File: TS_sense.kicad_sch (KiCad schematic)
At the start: 28 parts, among them U11 OPA355NA, U13 SFH617A-1X007T

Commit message: Changed Layout
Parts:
- added U16: TBA1-0511E, Converter_DCDC:Converter_DCDC_TRACO_TBA1-xxxxE_Single_THT, symbol Converter_DCDC:TBA1-0511E
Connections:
- net +5V_{iso}: now also U16.6 (+Vout)
- net GND: now also U16.2 (-Vin)
- net  HV+ renamed TS+
- net HV- renamed TS-
- net TS-: now also U16.4 (-Vout)
- new net +5V: U16.1 (+Vin)
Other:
- note added: "ISO 1.5kV"
- note added: "ISO 3750kV_{rms}"
- note added: "LVS"
- note added: "TS VOLTAGE AREA"
- note removed: "Footprint Check"

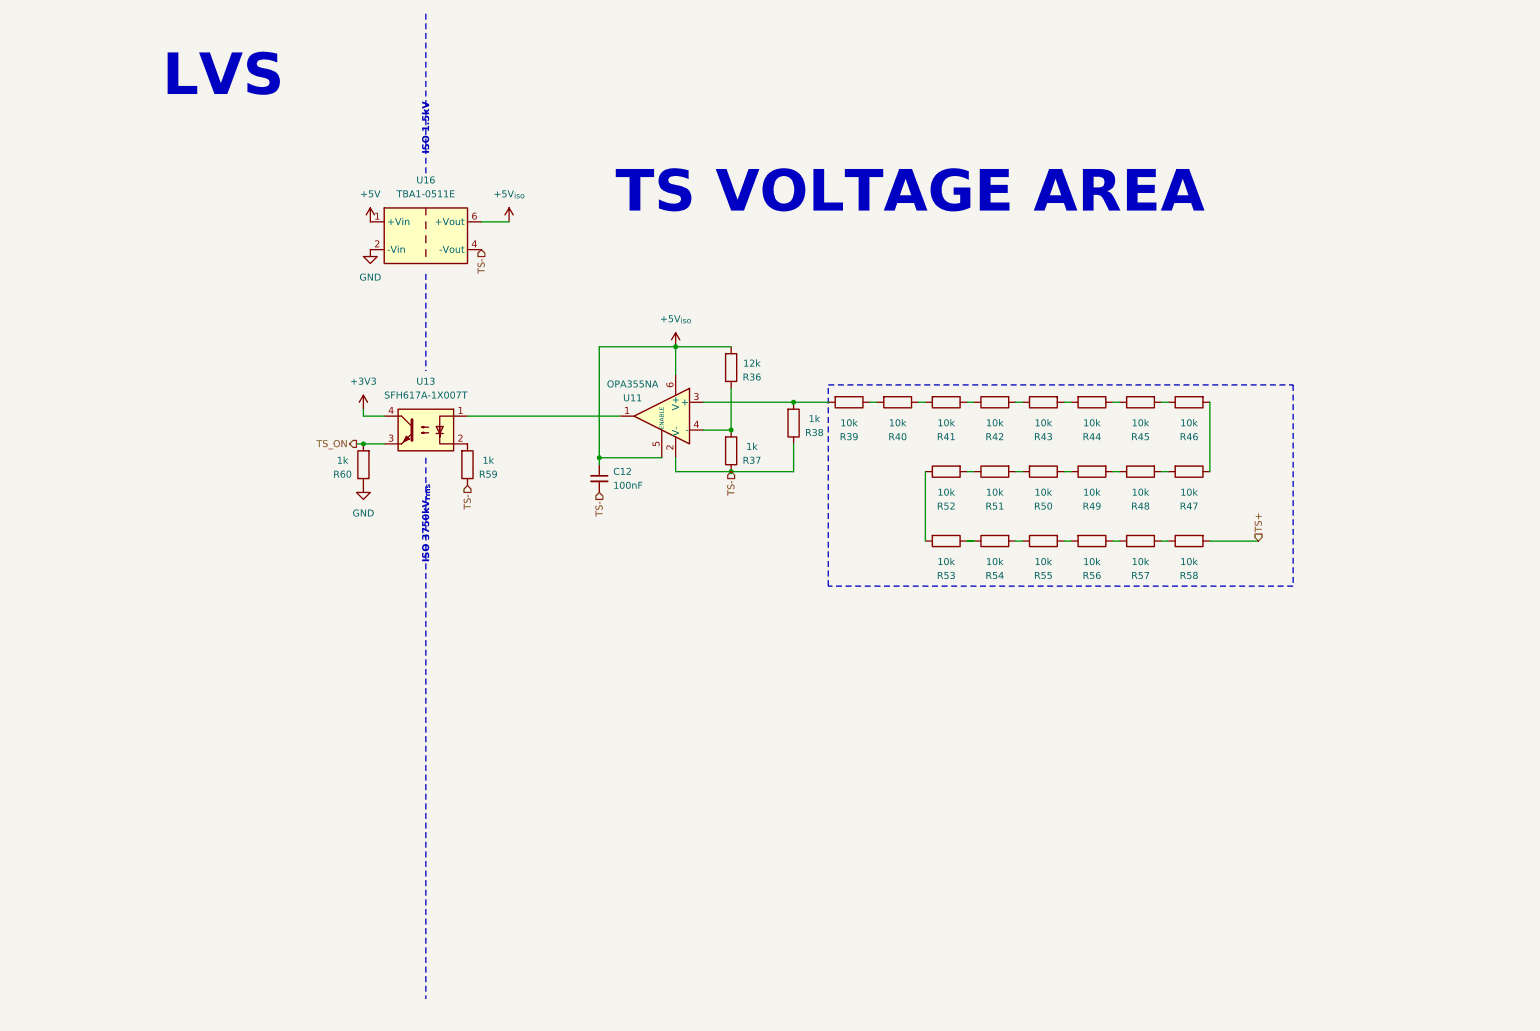
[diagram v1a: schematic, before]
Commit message: Added decoupling Caps
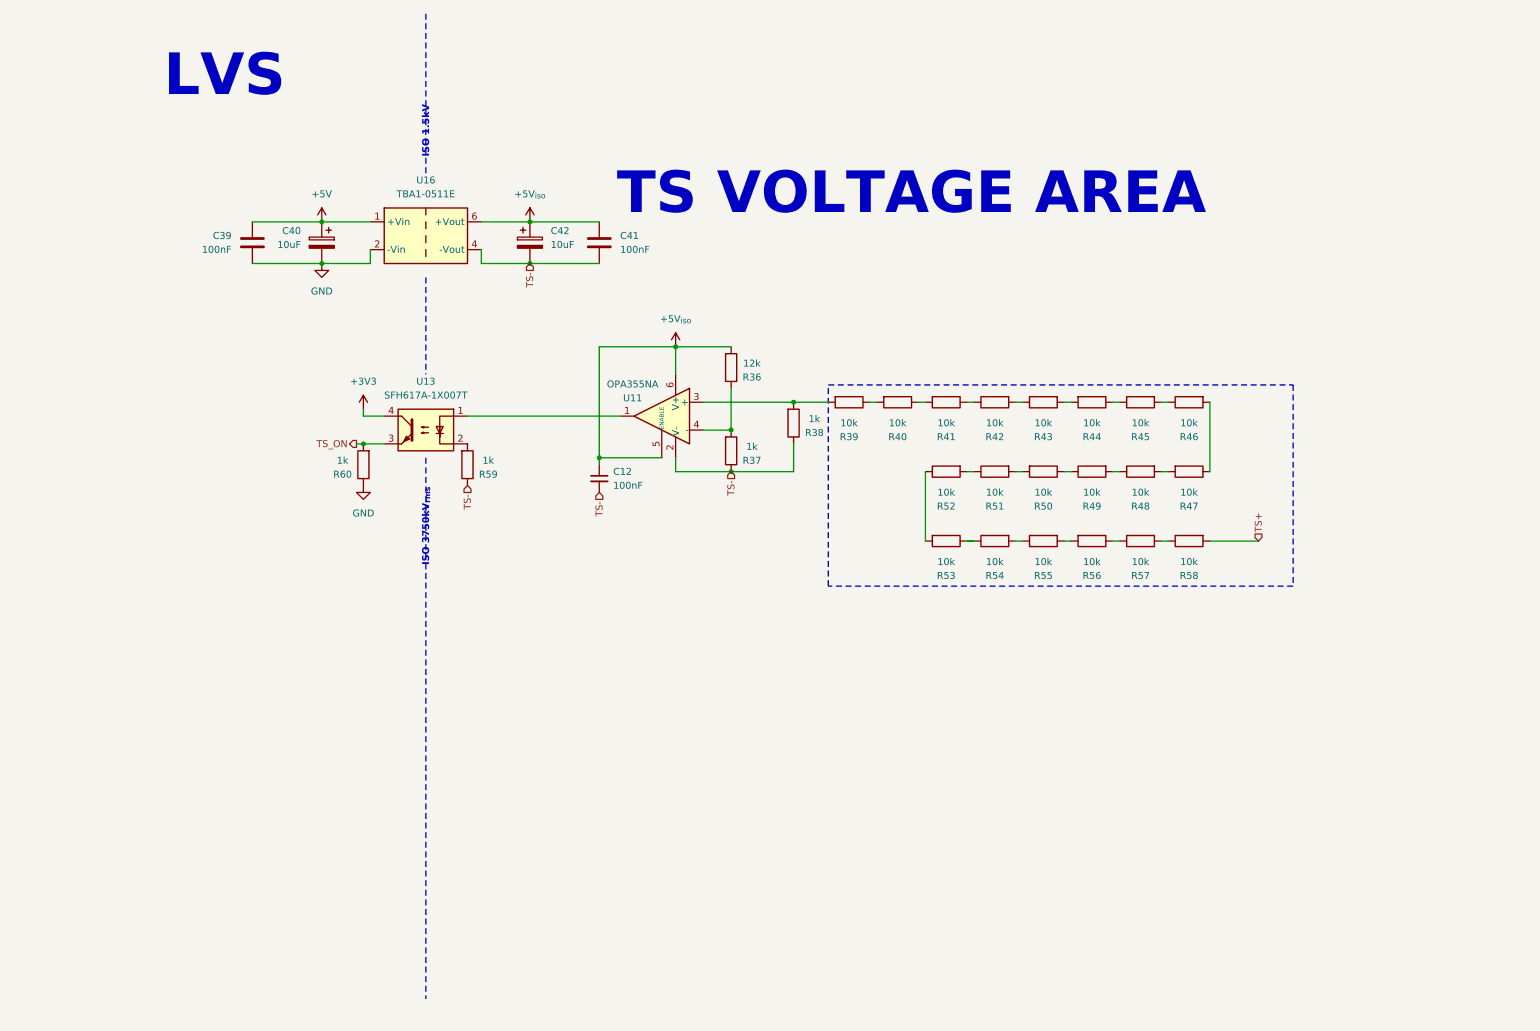
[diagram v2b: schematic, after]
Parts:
- added C39, C41: 100nF, symbol Device:C
- added C40, C42: 10uF, symbol Device:C_Polarized
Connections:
- net +5V: now also C39.1, C40.1
- net +5V_{iso}: now also C41.1, C42.1
- net GND: now also C39.2, C40.2
- net TS-: now also C41.2, C42.2

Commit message: Added Rules
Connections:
- net +3V3 is gone; now on net +5V: U13.4
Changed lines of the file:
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@@
 	(text "TS VOLTAGE AREA"
 		(exclude_from_sim no)
-		(at 171.45 45.72 0)
+		(at 175.006 24.13 0)
 		(effects
 			(font
@@
 	)
 	(symbol
-		(lib_id "power:+3V3")
+		(lib_id "power:+5V")
 		(at 71.12 85.09 0)
 		(unit 1)
@@
 			)
 		)
-		(property "Value" "+3V3"
+		(property "Value" "+5V"
 			(at 71.12 80.01 0)
 			(effects
@@
 			)
 		)
-		(property "Description" "Power symbol creates a global label with name \"+3V3\""
+		(property "Description" "Power symbol creates a global label with name \"+5V\""
 			(at 71.12 85.09 0)
 			(effects
@@
 		)
 		(instances
-			(project ""
+			(project "rpm_TSAL"
 				(path "/d61aec95-1a95-4bdc-98ef-7f05cebfb826/3d691545-fb91-40e8-bbf0-202d017ae861"
 					(reference "#PWR050")

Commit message: Submission Ready. ESF 15.07.24
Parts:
- removed R39, R40, R41, R42, R43, R44, R45, R46, R47, R48, R49, R50, R51, R52, R53, R54, R55, R56, R57, R58: 10k, Resistor_SMD:R_0603_1608Metric, symbol Device:R
- added R10, R11, R12, R13, R8, R9: 52k3, Resistor_SMD:R_0805_2012Metric, symbol Device:R
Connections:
- net TS+: now also R13.1
- net at R38.2, U11.3 (+): now also R8.2
- new net: R10.1, R11.1
- new net: R11.2, R12.1
- new net: R12.2, R13.2
- new net: R10.2, R9.1
- new net: R8.1, R9.2
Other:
- note added: "Resistor Datasheet"

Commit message: ⠀⠀⠀⠀⠀⠀⠀⠀⠀⠀⠀⠀⠀⠀⠀⠀⠀⠀⠀⠀⠀⠀⠀⠀⠀⠀⠀⠀⠀⠀⠀⠀⠀⠀⠀⠀⠀⣠⣤⣤⣤⡀⠀⠀⠀⠀⠀⠀⠀⠀⠀⠀⠀⠀⠀⠀⠀⠀⠀⠀⠀⠀⠀⠀⠀ ⠀⠀⠀⠀⠀⠀⠀⠀⠀⠀⠀⠀⠀⠀⠀⠀⠀⠀⠀⠀⠀⠀⠀⠀⠀⠀⠀⠀⠀⠀⠀⠀⠀⠀⣠⣶⣿⠟⠉⠉⠻⣿⡄⠀⠀⠀⠀⠀⠀⠀⠀⠀⠀⠀⠀⠀⠀⠀⠀⠀⠀⠀⠀⠀⠀ ⠀⠀⠀⠀⠀⠀⠀⠀⠀⠀⠀⠀⠀⠀⠀⠀⠀⠀⠀⠀⠀⠀⠀⠀⠀⠀⠀⠀⠀⠀⠀⢀⣤⣾⠿⠉⠀⠀⠀⠀⠀⠹⣿⡄⠀⠀⠀⠀⠀⠀⠀⠀⠀⠀⠀⠀⠀⠀⠀⠀⠀⠀⣀⣴⣾ ⠀⠀⠀⠀⠀⠀⠀⠀⠀⠀⠀⠀⠀⠀⠀⠀⠀⠀⠀⠀⠀⠀⠀⠀⠀⠀⠀⠀⠀⢀⣴⣿⠟⠁⠀⠀⠀⠀⠀⠀⠀⠀⣿⣿⠀⠀⠀⠀⠀⠀⠀⠀⠀⠀⠀⠀⠀⠀⠀⣀⣴⣾⡿⠛⠉ ⠀⠀⠀⠀⠀⠀⠀⠀⠀⠀⠀⠀⠀⠀⠀⠀⠀⠀⠀⠀⠀⠀⠀⠀⠀⠀⠀⢀⣴⣿⠟⠁⠀⠀⠀⠀⠀⠀⠀⠀⠀⠀⢸⣿⡆⠀⠀⠀⠀⠀⠀⠀⠀⠀⠀⠀⢀⣴⣾⡿⠟⠁⠀⠀⠀ ⠀⠀⠀⠀⠀⠀⠀⠀⠀⠀⠀⠀⠀⠀⠀⠀⠀⠀⠀⠀⠀⠀⠀⠀⢀⣀⣴⣿⡿⠃⠀⠀⠀⠀⠀⠀⠀⠀⠀⠀⠀⠀⢸⣿⣷⣶⣶⣦⣤⣤⣄⡀⠀⢀⣠⣾⣿⠿⠋⠀⠀⠀⠀⠀⣠ ⠀⠀⠀⠀⠀⠀⠀⠀⠀⠀⠀⠀⠀⠀⠀⠀⠀⠀⠀⠀⠀⠀⠀⣼⣿⣿⡿⠋⠀⠀⠀⠀⠀⠀⠀⠀⠀⠀⠀⣠⣤⠶⠞⣿⠟⠋⠉⠉⠙⣻⠿⢿⣿⣿⣿⠟⠁⠀⠀⠀⠀⠀⢀⡼⠁ ⠀⠀⠀⠀⠀⠀⠀⠀⠀⠀⠀⠀⠀⠀⠀⠀⠀⠀⠀⠀⠀⠀⢰⣿⠁⠛⠀⠀⠀⠀⠀⠀⠀⠀⠀⠀⠀⠀⣰⠟⠁⢠⡞⠁⠀⠀⠀⢀⡴⠋⠀⢀⡿⠋⠁⠀⠀⠀⠀⠀⠀⠀⡞⠁⠀ ⠀⠀⠀⠀⠀⠀⠀⠀⠀⠀⠀⠀⠀⠀⠀⠀⠀⠀⠀⠀⠀⣠⣼⣿⡄⠀⠀⠀⠀⠀⠀⠀⠀⠀⠀⠀⠀⣼⠃⠀⢠⠏⠀⠀⠀⠀⣰⠏⠀⠀⣠⠟⠀⠀⠀⠀⠀⠀⠀⠀⠀⢸⡥⠤⡀ ⠀⠀⠀⠀⠀⠀⠀⠀⠀⠀⠀⠀⠀⠀⠀⠀⠀⠀⠀⠀⣰⣿⠟⠁⠀⠀⠀⠀⠀⠀⠀⠀⠀⠀⠀⠀⠠⣇⠀⣠⡏⠀⠀⠀⠀⣼⠁⠀⠀⣰⠋⠀⠀⠀⠀⠀⠀⠀⠀⠀⠀⠀⢀⡴⠁ ⠀⠀⠀⠀⠀⠀⠀⠀⠀⠀⠀⠀⠀⠀⠀⠀⣀⣄⣄⣼⣿⠋⠀⠀⠀⠀⠀⠀⠀⠀⠀⠀⠀⠀⠀⠀⠀⢻⡶⠋⠀⠀⠀⠀⢸⣧⠀⠀⣴⠃⠀⠀⠀⠀⠀⠀⠀⠀⠀⠀⠀⠀⠘⢧⠀ ⠀⠀⠀⠀⠀⠀⠀⠀⢀⣀⣀⠀⠀⠀⠀⣾⡿⠿⣿⡿⠁⠀⠀⠀⠀⠀⠀⣠⣶⣶⣶⡀⠀⠀⠀⠀⠀⠀⠀⠀⠀⠀⠀⠀⠀⠙⠛⠛⠁⠀⠀⠀⠀⠀⠀⠀⠀⠀⠀⠀⠀⠀⠀⠈⠳ ⠀⠀⠀⠀⠀⠀⢀⣾⠿⠛⢿⣿⣷⣄⡀⣿⠃⠀⠈⠀⠀⠀⠀⠀⠀⢀⣾⣿⣿⣿⣿⣧⠀⠀⠀⠀⠀⠀⠀⠀⠀⠀⠀⠀⠀⠀⠀⠀⠀⠀⠀⠀⠀⠀⠀⠀⠀⠀⠀⠀⠀⠀⠀⠀⠀ ⠀⠀⠀⣠⣤⣦⣼⣿⠀⠀⠀⣿⣿⣿⣿⣿⣦⣀⠀⠀⠀⠀⠀⠀⠀⣿⣿⣿⣿⣿⣿⡿⠀⠀⠀⢀⣀⣀⣀⣀⡀⠀⠀⠀⠀⠀⠀⠀⠀⠀⠀⣤⣾⣿⣿⣿⣷⣄⠀⠀⠀⠀⠀⠀⠀ ⠀⣠⣾⡿⠋⠉⠉⠁⠀⠀⠀⠀⠉⢯⡙⠻⣿⣿⣷⣤⡀⠀⠀⠀⠀⢿⣿⣿⣿⣿⡿⠃⢀⡤⠖⠋⠉⠉⠉⠉⠉⠉⠒⠦⣄⠀⠀⠀⠀⠀⣾⣿⣿⣿⣿⣿⣿⣿⣧⠀⠀⠀⠀⠀⠀ ⣾⣿⠋⠀⠀⠀⠀⣀⣀⠀⠀⠀⠀⠀⠙⢦⣄⠉⠻⢿⣿⣷⣦⡀⠀⠈⠙⠛⠛⠋⠀⢰⠟⡇⠀⠀⠀⠀⠀⠀⠀⠀⠀⠀⠈⠳⣄⠀⠀⠀⣿⣿⣿⣿⣿⣿⣿⣿⣿⠀⠀⠀⠀⠀⠀ ⣿⡇⠀⠀⠀⣴⠟⣫⣿⣿⣄⠀⠀⠀⠀⡶⢌⡙⠶⣤⡈⠛⠿⣿⣷⣦⣀⠀⠀⠀⠀⡇⠀⢻⣄⠀⠀⣠⢷⠀⠀⠀⠀⠀⡶⠀⠘⡆⠀⠀⠻⣿⣿⣿⣿⣿⣿⣿⡟⠀⠀⠀⠀⠀⠀ ⣿⡇⠀⠀⢸⣟⢸⣿⣿⣿⣿⠀⠀⠀⠀⡇⠀⠈⠛⠦⣝⡳⢤⣈⠛⠻⣿⣷⣦⣀⠀⠀⠀⠀⠈⠙⠋⠁⠀⠛⠦⠤⠤⠚⠁⠀⠀⢳⠀⠀⠀⠈⠛⠿⠿⠿⠟⠋⠀⠀⠀⠀⠀⠀⠀ ⣿⡇⠀⠀⠈⢿⣞⣿⣿⣿⠏⠀⠀⠀⠀⡇⠀⠀⠀⠀⠀⠙⠳⢬⣛⠦⠀⠙⢻⣿⣷⣦⣀⠀⠀⠀⠀⠀⠀⠀⠀⠀⠀⠀⠀⠀⠀⡞⠀⠀⠀⠀⠀⠀⠀⠀⠀⠀⠀⠀⠀⠀⠀⠀⠀ ⣿⡇⠀⠀⠀⠀⠉⠛⠋⠁⠀⠀⠀⠀⠀⡇⠀⠀⠀⠀⠀⠀⠀⠀⠈⠁⠀⠀⠈⣿⠉⢻⣿⣷⣦⣀⠀⠀⠀⠀⠀⠀⠀⠀⠀⢀⡼⠁⠀⠀⠀⠀⠀⠀⠀⠀⠀⠀⠀⠀⠀⠀⠀⠀⠀ ⣿⡇⠀⠀⠀⠀⠀⣠⣄⠀⠀⢰⠶⠒⠒⢧⣄⡀⠀⠀⠀⠀⠀⠀⠀⠀⠀⠀⠀⣿⠀⢸⡇⢸⡟⢿⣷⣦⣴⣶⣶⣶⣶⣤⣔⠋⠀⠀⠀⠀⠀⠀⠀⠀⠀⠀⠀⠀⠀⠀⠀⠀⠀⠀⠀ ⣿⡇⠀⠀⣤⠀⠀⠿⠿⠁⢀⡿⠀⠀⠀⡄⠈⠙⡷⢦⣄⡀⠀⠀⠀⠀⠀⠀⠀⣿⠀⢸⡇⢸⡇⠀⣿⠙⣿⣿⣉⠉⠙⠿⣿⣧⠀⠀⠀⠀⠀⠀⠀⠀⠀⠀⠀⠀⠀⠀⠀⠀⠀⠀⠀ ⣿⡇⠀⠀⠙⠷⢤⣀⣠⠴⠛⠁⠀⠀⠀⠇⠀⠀⡇⢸⡏⢹⡷⢦⣄⡀⠀⠀⠀⣿⡀⢸⡇⢸⡇⠀⡟⠀⢸⠀⢹⡷⢦⣄⣘⣿⡆⠀⠀⠀⠀⠀⠀⠀⠀⠀⠀⠀⠀⠀⠀⠀⠀⠀⠀ ⣿⣿⠢⣤⡀⠀⠀⠀⠀⠀⠀⣠⠾⣿⣿⡷⣤⣀⡇⠸⡇⢸⡇⢸⠉⠙⠳⢦⣄⡻⢿⣾⣧⣸⣧⠀⡇⠀⢸⠀⢸⡇⢤⣈⠙⠻⣿⣆⠀⠀⠀⠀⠀⠀⠀⠀⠀⠀⠀⠀⠀⠀⠀⠀⠀ ⢹⣿⣷⣌⡉⠛⠲⢶⣶⠖⠛⠛⢶⣄⡉⠛⠿⣽⣿⣶⣧⣸⡇⢸⠀⠀⠀⠀⠈⠙⠲⢮⣝⠻⣿⣷⣷⣄⣸⠀⢸⡇⠀⠈⠁⠀⢸⣿⠀⠀⠀⠀⠀⠀⠀⠀⠀⠀⠀⠀⠀⠀⠀⠀⠀ ⠀⠈⠙⠻⢿⣷⣶⣤⣉⡻⢶⣄⣀⠈⠙⠳⢦⣈⡉⠻⢿⣿⣷⣾⣦⡀⠀⠀⠀⠀⠀⠀⠈⠙⠲⢭⣛⠿⣿⣷⣼⡇⠀⠀⠀⠀⠈⣿⡇⠀⠀⠀⠀⠀⠀⣀⠀⠀⠀⠀⠀⠀⠀⠀⣀ ⠀⠀⠀⠀⠀⠈⠙⠻⢿⣿⣷⣶⣽⣻⡦⠀⠀⠈⠙⠷⣦⣌⡙⠻⢿⣟⣷⣤⣀⠀⠀⠀⠀⠀⠀⠀⠈⠙⠳⢯⣻⡇⠀⠀⠀⠀⠀⢸⣿⠀⣀⠀⠀⠀⠀⠈⠳⣄⠀⠀⠀⢀⡏⠙⠛ ⠀⠀⠀⠀⠀⠀⠀⠀⠀⠈⠛⠻⢿⣿⣿⣿⣶⣤⣤⣤⣀⣈⠛⠷⣤⣈⡛⠷⢽⡻⢶⣄⣀⠀⠀⠀⠀⠀⠀⠀⠈⠛⠳⢤⣀⠀⠀⢸⣿⡀⠈⠳⢤⣀⣀⣰⠃⠈⠛⠶⠶⠿⠃⠀⠀ ⠀⠀⠀⠀⠀⠀⠀⠀⠀⠀⠀⠀⠀⢈⣿⡿⠛⠉⠙⠛⠛⠻⢷⣦⣄⣩⣿⠶⠖⠛⠛⠛⠛⠛⠛⠿⢷⣶⣦⣄⠀⠀⠀⠀⠉⢻⣶⣿⣿⠇⠀⠀⠀⠉⠉⠀⠀⠀⠀⠀⠀⠀⠀⠀⠀ ⠀⠀⠀⠀⠀⠀⠀⠀⠀⠀⠀⠀⠀⣼⣿⠁⠀⠀⠀⠀⠀⠀⠀⣿⣿⠋⠀⠀⠀⠀⠀⣠⠖⠂⠀⠀⠀⠈⠙⠿⣿⣦⡄⠀⠀⣸⣿⠟⠋⠀⠀⠀⠀⠀⠀⠀⠀⠀⠀⠀⠀⠀⠀⠀⠀ ⠀⠀⠀⠀⠀⠀⠀⠀⠀⠀⠀⠀⢰⣿⡟⠀⠀⠀⠀⠀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
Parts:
- C39, C40, C41, C42: footprint (none) -> Capacitor_SMD:C_0603_1608Metric
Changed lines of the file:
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@@
 			)
 		)
-		(property "Footprint" ""
+		(property "Footprint" "Capacitor_SMD:C_0603_1608Metric"
 			(at 115.2652 58.42 0)
 			(effects
@@
 			)
 		)
-		(property "Footprint" ""
+		(property "Footprint" "Capacitor_SMD:C_0603_1608Metric"
 			(at 62.5348 58.42 0)
 			(effects
@@
 			)
 		)
-		(property "Footprint" ""
+		(property "Footprint" "Capacitor_SMD:C_0603_1608Metric"
 			(at 49.8348 58.42 0)
 			(effects
@@
 			)
 		)
-		(property "Footprint" ""
+		(property "Footprint" "Capacitor_SMD:C_0603_1608Metric"
 			(at 102.5652 58.42 0)
 			(effects

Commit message: TSAL Rev 0.2
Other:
- moved on the sheet: R38
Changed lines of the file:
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@@
 		(title "TSAL")
 		(date "2024-07-11")
-		(rev "V0.1")
+		(rev "V0.2")
 		(company "Team RPM - UAS Münster")
 		(comment 1 "Luca Sapion")
@@
 	)
 	(junction
-		(at 138.43 96.52)
-		(diameter 0)
-		(color 0 0 0 0)
-	)
-	(junction
 		(at 71.12 91.44)
 		(diameter 0)
@@
 	)
 	(junction
+		(at 138.43 97.79)
+		(diameter 0)
+		(color 0 0 0 0)
+	)
+	(junction
 		(at 101.6 50.8)
 		(diameter 0)
@@
 	(wire
 		(pts
+			(xy 138.43 97.79) (xy 138.43 96.52)
+		)
+		(stroke
+			(width 0)
+			(type default)
+		)
+	)
+	(wire
+		(pts
 			(xy 92.71 50.8) (xy 101.6 50.8)
 		)
@@
 	(wire
 		(pts
+			(xy 138.43 100.33) (xy 138.43 97.79)
+		)
+		(stroke
+			(width 0)
+			(type default)
+		)
+	)
+	(wire
+		(pts
+			(xy 149.86 86.36) (xy 149.86 83.82)
+		)
+		(stroke
+			(width 0)
+			(type default)
+		)
+	)
+	(wire
+		(pts
 			(xy 125.73 93.98) (xy 114.3 93.98)
 		)
@@
 	(wire
 		(pts
-			(xy 128.27 93.98) (xy 128.27 96.52)
+			(xy 128.27 93.98) (xy 128.27 97.79)
 		)
 		(stroke
@@
 	(wire
 		(pts
-			(xy 128.27 96.52) (xy 138.43 96.52)
+			(xy 128.27 97.79) (xy 138.43 97.79)
 		)
 		(stroke
@@
 	(wire
 		(pts
-			(xy 138.43 96.52) (xy 149.86 96.52)
+			(xy 138.43 97.79) (xy 149.86 97.79)
 		)
 		(stroke
@@
 	(wire
 		(pts
-			(xy 149.86 96.52) (xy 149.86 91.44)
+			(xy 149.86 97.79) (xy 149.86 93.98)
 		)
 		(stroke
@@
 	(hierarchical_label "TS-"
 		(shape input)
-		(at 138.43 96.52 270)
+		(at 138.43 100.33 270)
 		(fields_autoplaced yes)
 		(effects
@@
 	(symbol
 		(lib_id "Device:R")
-		(at 149.86 87.63 0)
+		(at 149.86 90.17 0)
 		(mirror x)
 		(unit 1)
@@
 		(dnp no)
 		(property "Reference" "R38"
+			(at 153.67 91.948 0)
+			(effects
+				(font
+					(size 1.27 1.27)
+				)
+			)
+		)
+		(property "Value" "1k"
 			(at 153.67 89.408 0)
 			(effects
@@
 			)
 		)
-		(property "Value" "1k"
-			(at 153.67 86.868 0)
-			(effects
-				(font
-					(size 1.27 1.27)
-				)
-			)
-		)
 		(property "Footprint" "Resistor_SMD:R_0603_1608Metric"
-			(at 148.082 87.63 90)
+			(at 148.082 90.17 90)
 			(effects
 				(font
@@
 		)
 		(property "Datasheet" "~"
-			(at 149.86 87.63 0)
+			(at 149.86 90.17 0)
 			(effects
 				(font
@@
 		)
 		(property "Description" "Resistor"
-			(at 149.86 87.63 0)
-			(effects
-				(font
+			(at 149.86 90.17 0)
+			(effects
+				(font

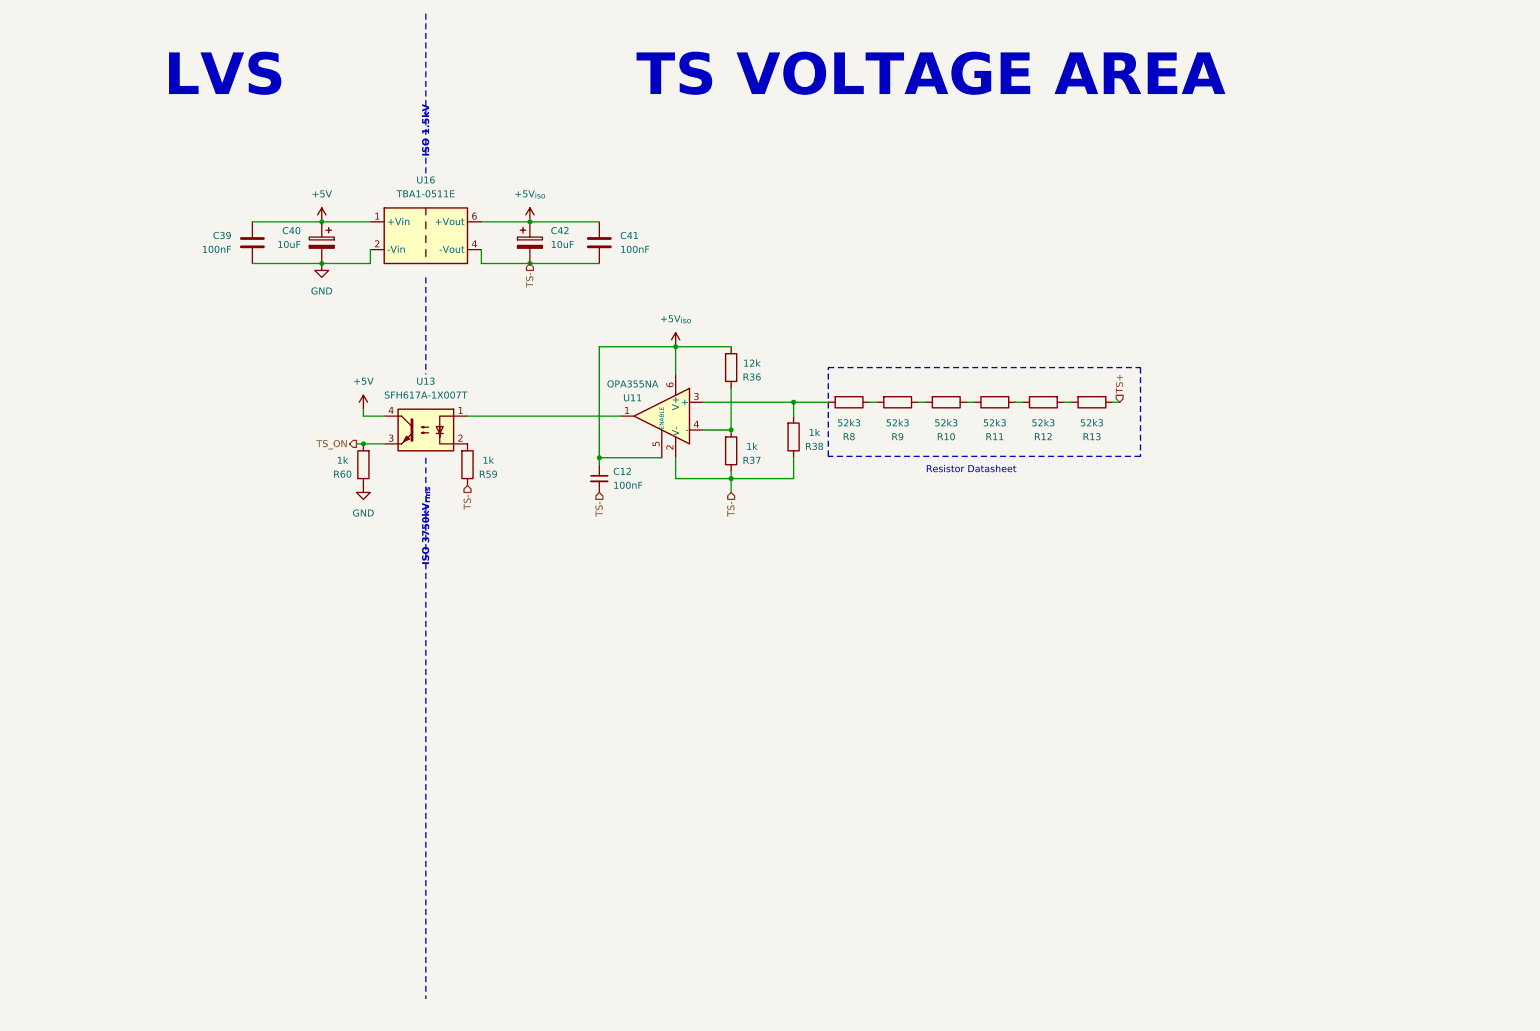
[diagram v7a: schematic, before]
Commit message: Added TSAC Indicator with PSU
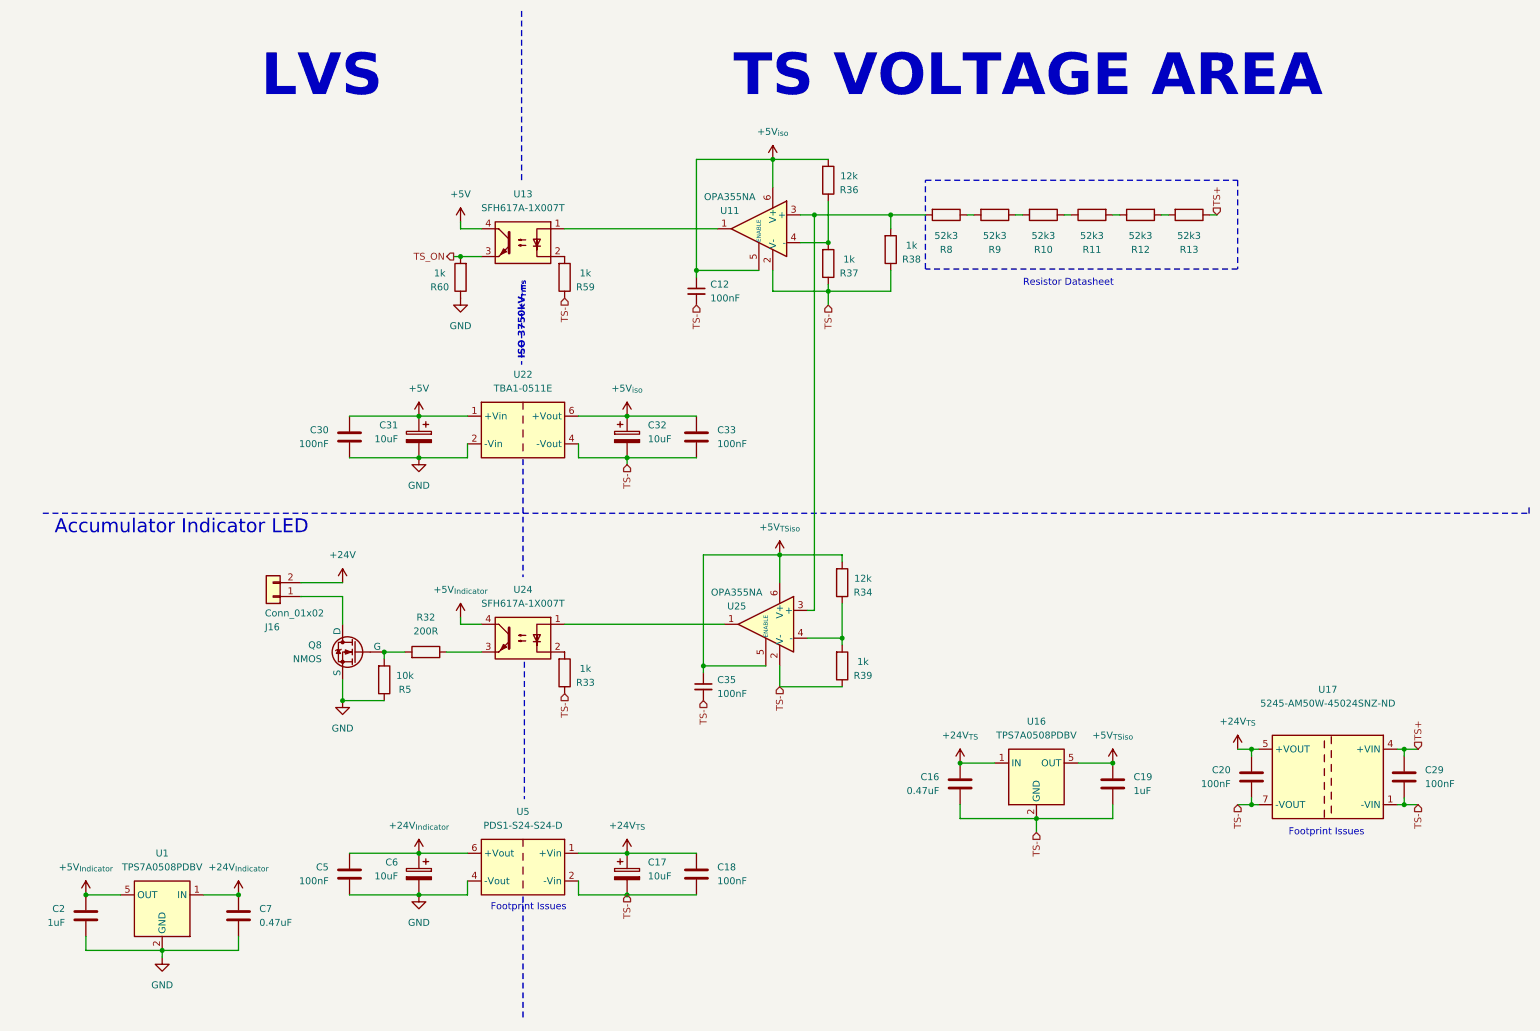
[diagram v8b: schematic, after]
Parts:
- removed C39, C41: 100nF, Capacitor_SMD:C_0603_1608Metric, symbol Device:C
- removed C40, C42: 10uF, Capacitor_SMD:C_0603_1608Metric, symbol Device:C_Polarized
- removed U16: TBA1-0511E, Converter_DCDC:Converter_DCDC_TRACO_TBA1-xxxxE_Single_THT, symbol Converter_DCDC:TBA1-0511E
- added C16, C7: 0.47uF, Capacitor_SMD:C_0603_1608Metric, symbol Device:C
- added C17, C31, C32, C6: 10uF, Capacitor_SMD:C_0603_1608Metric, symbol Device:C_Polarized
- added C18, C20, C29, C30, C33, C5: 100nF, Capacitor_SMD:C_0603_1608Metric, symbol Device:C
- added C19, C2: 1uF, Capacitor_SMD:C_0603_1608Metric, symbol Device:C
- added C35: 100nF, Capacitor_SMD:C_0603_1608Metric, symbol Device:C_Small
- added J16: Conn_01x02, wuerth_conn:66200211024, symbol Connector_Generic:Conn_01x02
- added Q8: NMOS, Package_TO_SOT_SMD:SOT-23-3, symbol Simulation_SPICE:NMOS
- added R32: 200R, symbol Device:R
- added R33, R39: 1k, Resistor_SMD:R_0603_1608Metric, symbol Device:R
- added R34: 12k, Resistor_SMD:R_0603_1608Metric, symbol Device:R
- added R5: 10k, Resistor_SMD:R_0603_1608Metric, symbol Device:R
- added U1, U16: TPS7A0508PDBV, Package_TO_SOT_SMD:SOT-23-5, symbol Regulator_Linear:TPS7A0508PDBV
- added U17: 5245-AM50W-45024SNZ-ND, Converter_DCDC:Converter_DCDC_Murata_CRE1xxxxxxDC_THT, symbol Regulator_Switching:CRE1S0505DC
- added U22: TBA1-0511E, Converter_DCDC:Converter_DCDC_TRACO_TBA1-xxxxE_Single_THT, symbol Converter_DCDC:TBA1-0511E
- added U24: SFH617A-1X007T, Package_DIP:SMDIP-4_W9.53mm_Clearance8mm, symbol Isolator:SFH617A-1X007T
- added U25: OPA355NA, Package_TO_SOT_SMD:SOT-23-6, symbol Amplifier_Operational:OPA355NA
- added U5: PDS1-S24-S24-D, Converter_DCDC:Converter_DCDC_TRACO_TBA1-xxxxE_Single_THT, symbol Converter_DCDC:TBA1-0511E
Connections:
- net +5V: now also C30.1, C31.1, U22.1 (+Vin)
- net +5V_{iso}: now also C32.1, C33.1, U22.6 (+Vout)
- net GND: now also C2.2, C30.2, C31.2, C5.2, C6.2, C7.2, Q8.3 (S), R5.1, U1.2 (GND), U22.2 (-Vin), U5.4 (-Vout)
- net TS+: now also C29.1, U17.4 (+VIN)
- net TS-: now also C16.2, C17.2, C18.2, C19.2, C20.2, C29.2, C32.2, C33.2, C35.2, R33.1, R39.1, U16.2 (GND), U17.1 (-VIN), U17.7 (-VOUT), U22.4 (-Vout), U25.2 (V-), U5.2 (-Vin)
- net at R38.2, R8.2, U11.3 (+): now also U25.3 (+)
- new net: U24.1, U25.1
- new net: R34.1, R39.2, U25.4 (-)
- new net: R33.2, U24.2
- new net: Q8.2 (G), R32.2, R5.2
- new net: R32.1, U24.3
- new net: J16.1 (Pin_1), Q8.1 (D)
- new net +24V: J16.2 (Pin_2)
- new net +24V_{Indicator}: C5.1, C6.1, C7.1, U1.1 (IN), U5.6 (+Vout)
- new net +24V_{TS}: C16.1, C17.1, C18.1, C20.1, U16.1 (IN), U17.5 (+VOUT), U5.1 (+Vin)
- new net +5V_{Indicator}: C2.1, U1.5 (OUT), U24.4
- new net +5V_{TSiso}: C19.1, C35.1, R34.2, U16.5 (OUT), U25.5 (ENABLE), U25.6 (V+)
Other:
- note added: "Accumulator Indicator LED"
- note added: "Footprint Issues"
- note removed: "ISO 1.5kV"
- moved on the sheet: C12, R10, R11, R12, R13, R36, R37, R38, R59, R60, R8, R9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
